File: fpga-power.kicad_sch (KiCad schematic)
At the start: 118 parts, among them U3002 XC7K160T-FFG676

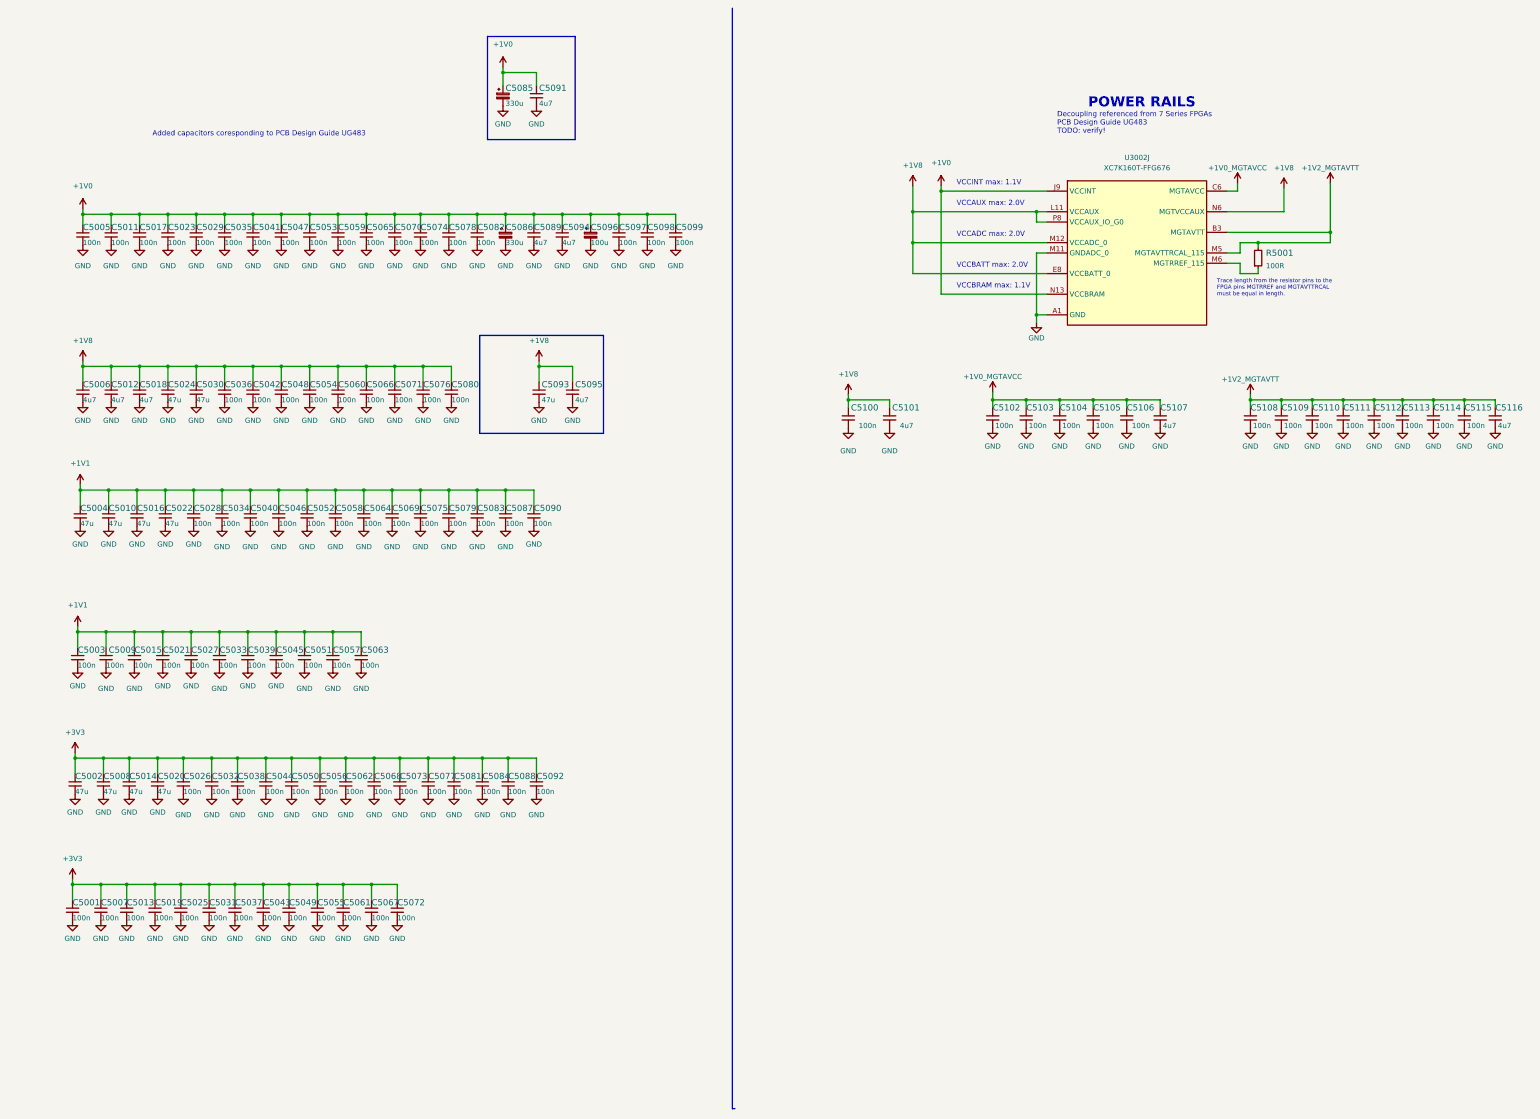
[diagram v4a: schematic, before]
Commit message: Create FPGA decoupling, start creating power planes
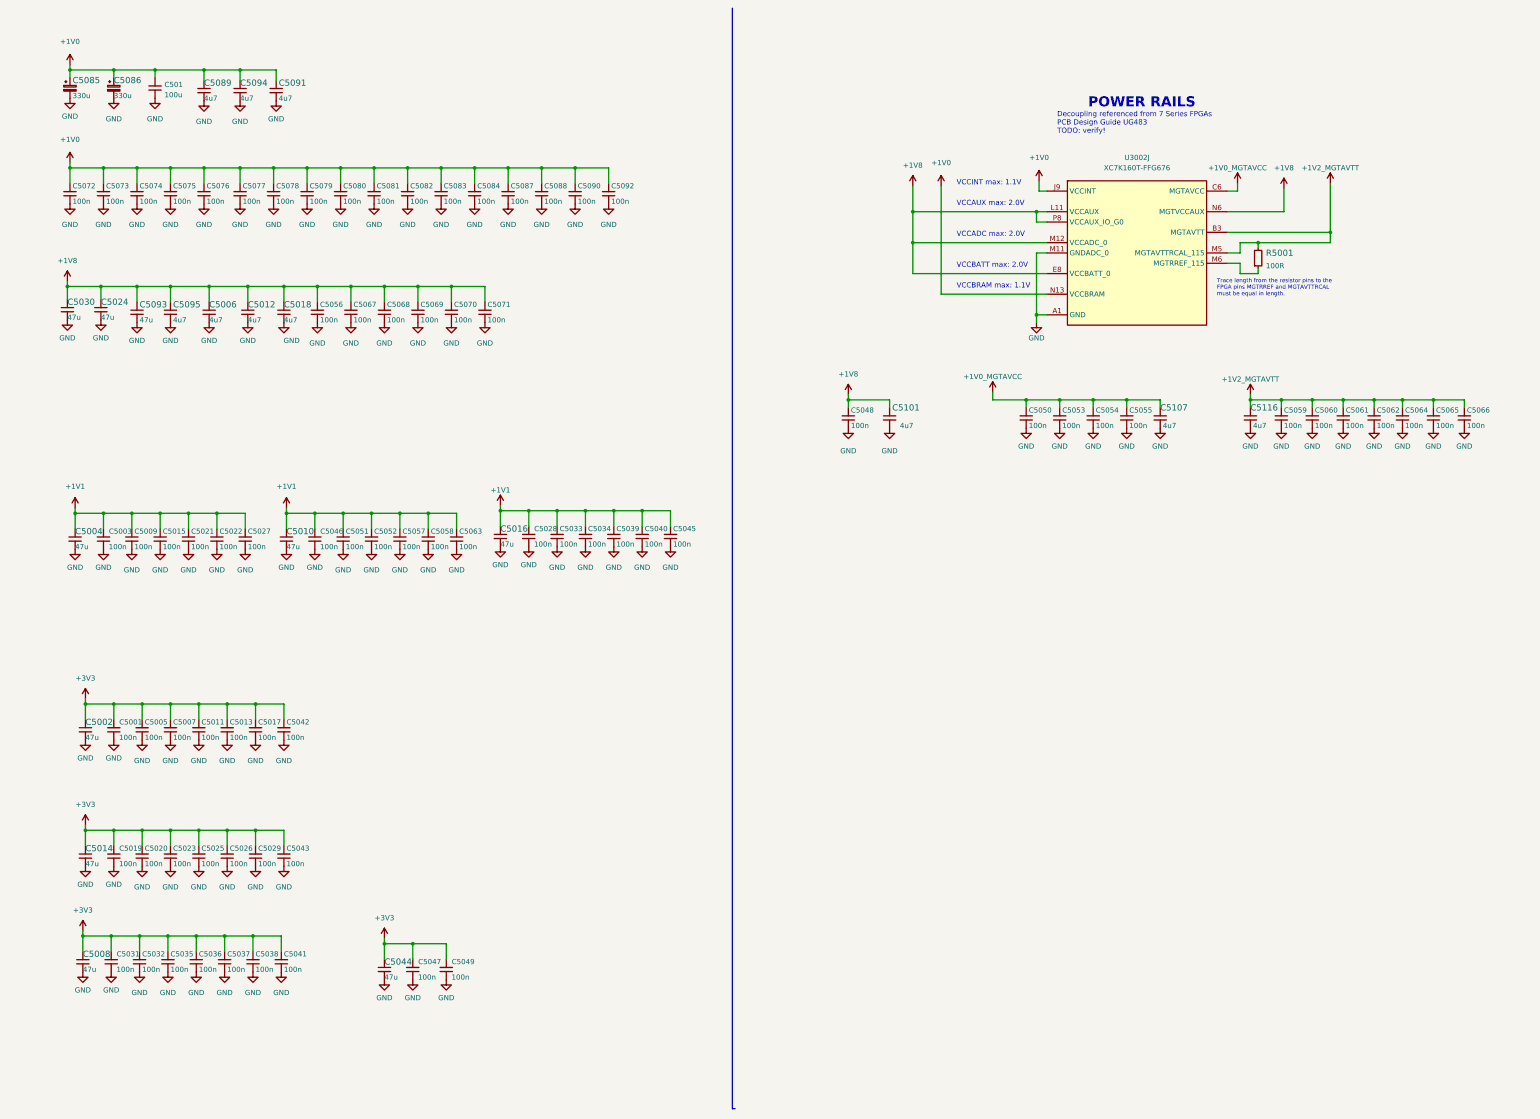
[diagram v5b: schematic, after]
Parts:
- removed C5001, C5003, C5005, C5007, C5009, C5011, C5013, C5015, C5017, C5019, C5021, C5023, C5025, C5026, C5027, C5028, C5029, C5031, C5032, C5033, C5034, C5035, C5036, C5037, C5038, C5039, C5040, C5041, C5042, C5043, C5044, C5045, C5046, C5047, C5048, C5049, C5050, C5051, C5052, C5053, C5054, C5055, C5056, C5057, C5058, C5059, C5060, C5061, C5062, C5063, C5064, C5065, C5066, C5067, C5068, C5069, C5070, C5071, C5072, C5073, C5074, C5075, C5076, C5077, C5078, C5079, C5080, C5081, C5082, C5083, C5084, C5087, C5088, C5092, C5097, C5098, C5099, C5100, C5102, C5103, C5104, C5105, C5106, C5109, C5110, C5111, C5112, C5113, C5114, C5115: C_100n_0201, data-center-rdimm-ddr4-tester-footprints:C_0201, symbol data-center-rdimm-ddr4-tester:C_100n_0201
- removed C5020, C5022: C_47u_0603, data-center-rdimm-ddr4-tester-footprints:C_0603_1608Metric, symbol data-center-rdimm-ddr4-tester:C_47u_0603
- removed C5090, C5108: C_100n_0402, data-center-rdimm-ddr4-tester-footprints:C_0402_1005Metric, symbol data-center-rdimm-ddr4-tester:C_100n_0402
- removed C5096: C_100u_KEMET_A, data-center-rdimm-ddr4-tester-footprints:KEMET_A, symbol data-center-rdimm-ddr4-tester:C_100u_KEMET_A
- added C5001, C5003, C5005, C5007, C5009, C5011, C5013, C5015, C5017, C5019, C5020, C5021, C5022, C5023, C5025, C5026, C5027, C5028, C5029, C5031, C5032, C5033, C5034, C5035, C5036, C5037, C5038, C5039, C5040, C5041, C5042, C5043, C5045, C5046, C5047, C5048, C5049, C5050, C5051, C5052, C5053, C5054, C5055, C5056, C5057, C5058, C5059, C5060, C5061, C5062, C5063, C5064, C5065, C5066, C5067, C5068, C5069, C5070, C5071, C5072, C5073, C5074, C5075, C5076, C5077, C5078, C5079, C5080, C5081, C5082, C5083, C5084, C5087, C5088, C5090, C5092: C_100n_0402, antmicro-footprints:C_0402_1005Metric_EIA, symbol antmicroCapacitors0402:C_100n_0402
- added C501: C_100u_0805, antmicro-footprints:C_0805_2012Metric, symbol antmicroCapacitorsmisc:C_100u_0805
- added C5044: C_47u_0603, data-center-rdimm-ddr4-tester-footprints:C_0603_1608Metric, symbol data-center-rdimm-ddr4-tester:C_47u_0603
- C5006, C5012, C5018, C5089, C5091, C5094, C5095, C5101, C5107, C5116: footprint data-center-rdimm-ddr4-tester-footprints:C_0402_1005Metric -> antmicro-footprints:C_0402_1005Metric_EIA
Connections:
- net +1V0: now also C501.2, C5072.2, C5073.2, C5074.2, C5075.2, C5076.2, C5077.2, C5078.2, C5079.2, C5080.2, C5081.2, C5082.2, C5083.2, C5084.2, C5087.2, C5088.2, C5090.2, C5092.2
- net +1V0_MGTAVCC: now also C5050.2, C5053.2, C5054.2, C5055.2
- net +1V1: now also C5003.2, C5009.2, C5015.2, C5021.2, C5022.2, C5027.2, C5028.2, C5033.2, C5034.2, C5039.2, C5040.2, C5045.2, C5046.2, C5051.2, C5052.2, C5057.2, C5058.2, C5063.2
- net +1V2_MGTAVTT: now also C5059.2, C5060.2, C5061.2, C5062.2, C5064.2, C5065.2, C5066.2
- net +1V8: now also C5048.2, C5056.2, C5067.2, C5068.2, C5069.2, C5070.2, C5071.2
- net +3V3: now also C5001.2, C5005.2, C5007.2, C5011.2, C5013.2, C5017.2, C5019.2, C5020.2, C5023.2, C5025.2, C5026.2, C5029.2, C5031.2, C5032.2, C5035.2, C5036.2, C5037.2, C5038.2, C5041.2, C5042.2, C5043.2, C5044.1, C5047.2, C5049.2
- net GND: now also C5001.1, C5003.1, C5005.1, C5007.1, C5009.1, C501.1, C5011.1, C5013.1, C5015.1, C5017.1, C5019.1, C5020.1, C5021.1, C5022.1, C5023.1, C5025.1, C5026.1, C5027.1, C5028.1, C5029.1, C5031.1, C5032.1, C5033.1, C5034.1, C5035.1, C5036.1, C5037.1, C5038.1, C5039.1, C5040.1, C5041.1, C5042.1, C5043.1, C5044.2, C5045.1, C5046.1, C5047.1, C5048.1, C5049.1, C5050.1, C5051.1, C5052.1, C5053.1, C5054.1, C5055.1, C5056.1, C5057.1, C5058.1, C5059.1, C5060.1, C5061.1, C5062.1, C5063.1, C5064.1, C5065.1, C5066.1, C5067.1, C5068.1, C5069.1, C5070.1, C5071.1, C5072.1, C5073.1, C5074.1, C5075.1, C5076.1, C5077.1, C5078.1, C5079.1, C5080.1, C5081.1, C5082.1, C5083.1, C5084.1, C5087.1, C5088.1, C5090.1, C5092.1
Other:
- note removed: "Added capacitors coresponding to PCB Design Guide UG483"
- moved on the sheet: C5002, C5004, C5006, C5008, C5010, C5012, C5014, C5016, C5018, C5024, C5030, C5085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

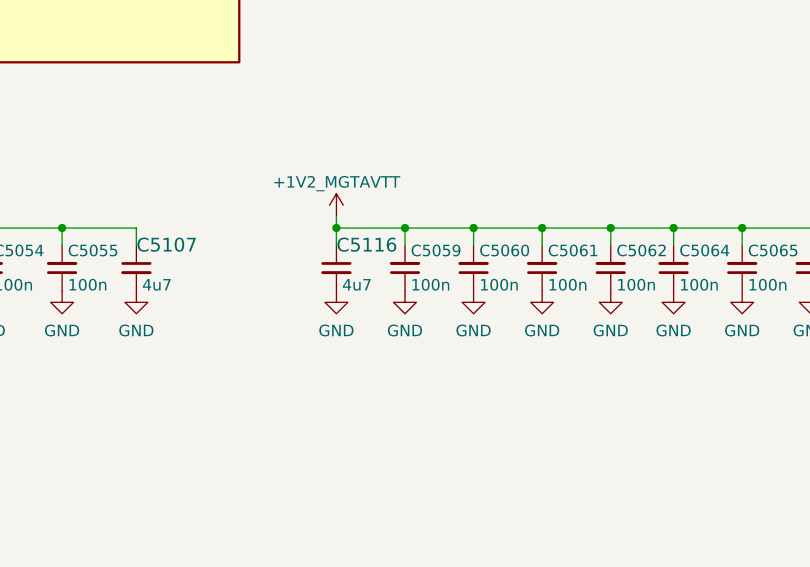
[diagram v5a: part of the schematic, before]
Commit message: Improve DDR assigment, connect ECC to remaining pins, cleanup not used components, continue placement of misc. components
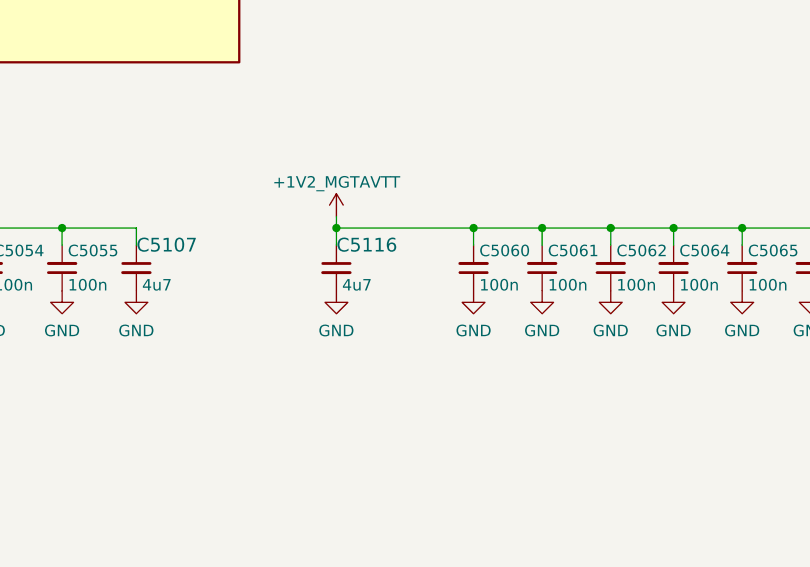
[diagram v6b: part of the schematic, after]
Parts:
- removed C5059: C_100n_0402, antmicro-footprints:C_0402_1005Metric_EIA, symbol antmicroCapacitors0402:C_100n_0402
- R5001: footprint data-center-rdimm-ddr4-tester-footprints:R_0402_1005Metric -> antmicro-footprints:R_0402_1005Metric_EIA
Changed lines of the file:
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@@
   (junction (at 52.705 184.15) (diameter 0) (color 0 0 0 0)
   )
-  (junction (at 326.39 109.22) (diameter 0) (color 0 0 0 0)
-  )
   (junction (at 44.45 81.28) (diameter 0) (color 0 0 0 0)
   )
@@
     (stroke (width 0) (type default) (color 0 0 0 0))
   )
-  (wire (pts (xy 326.39 109.22) (xy 334.01 109.22))
-    (stroke (width 0) (type default) (color 0 0 0 0))
-  )
   (wire (pts (xy 140.97 136.525) (xy 133.985 136.525))
     (stroke (width 0) (type default) (color 0 0 0 0))
@@
     (stroke (width 0) (type default) (color 0 0 0 0))
   )
-  (wire (pts (xy 318.77 109.22) (xy 326.39 109.22))
+  (wire (pts (xy 318.77 109.22) (xy 334.01 109.22))
     (stroke (width 0) (type default) (color 0 0 0 0))
   )
@@
     (stroke (width 0) (type default) (color 0 0 0 0))
   )
-  (wire (pts (xy 326.39 109.22) (xy 326.39 111.125))
-    (stroke (width 0) (type default) (color 0 0 0 0))
-  )
   (wire (pts (xy 356.235 109.22) (xy 363.855 109.22))
     (stroke (width 0) (type default) (color 0 0 0 0))
@@
     (pin "1")
   )
-  (symbol (lib_id "antmicroCapacitors0402:C_100n_0402") (at 326.39 116.205 90) (unit 1)
-    (in_bom yes) (on_board yes)
-    (property "Reference" "C5059" (id 0) (at 327.025 111.76 90)
-      (effects (font (size 1.27 1.27) (thickness 0.15)) (justify right))
-    )
-    (property "Value" "C_100n_0402" (id 1) (at 336.55 95.885 0)
-      (effects (font (size 1.27 1.27) (thickness 0.15)) (justify left bottom) hide)
-    )
-    (property "Footprint" "antmicro-footprints:C_0402_1005Metric_EIA" (id 2) (at 339.09 95.885 0)
-      (effects (font (size 1.27 1.27) (thickness 0.15)) (justify left bottom) hide)
-    )
-    (property "Datasheet" "https://www.murata.com/products/productdetail?partno=GRM155R61H104KE14%23" (id 3) (at 341.63 95.885 0)
-      (effects (font (size 1.27 1.27) (thickness 0.15)) (justify left bottom) hide)
-    )
-    (property "MPN" "GRM155R61H104KE14D" (id 4) (at 344.17 95.885 0)
-      (effects (font (size 1.27 1.27) (thickness 0.15)) (justify left bottom) hide)
-    )
-    (property "Manufacturer" "Murata" (id 5) (at 346.71 95.885 0)
-      (effects (font (size 1.27 1.27) (thickness 0.15)) (justify left bottom) hide)
-    )
-    (property "License" "Apache-2.0" (id 6) (at 349.25 95.885 0)
-      (effects (font (size 1.27 1.27) (thickness 0.15)) (justify left bottom) hide)
-    )
-    (property "Author" "Antmicro" (id 7) (at 351.79 95.885 0)
-      (effects (font (size 1.27 1.27) (thickness 0.15)) (justify left bottom) hide)
-    )
-    (property "Val" "100n" (id 8) (at 327.025 115.57 90)
-      (effects (font (size 1.27 1.27) (thickness 0.15)) (justify right))
-    )
-    (property "Voltage" "50V" (id 9) (at 354.33 95.885 0)
-      (effects (font (size 1.27 1.27)) (justify left bottom) hide)
-    )
-    (property "Dielectric" "X5R" (id 10) (at 356.87 95.885 0)
-      (effects (font (size 1.27 1.27)) (justify left bottom) hide)
-    )
-    (pin "1")
-    (pin "2")
-  )
   (symbol (lib_id "data-center-rdimm-ddr4-tester:GND") (at 52.705 60.96 0) (unit 1)
     (in_bom yes) (on_board yes) (fields_autoplaced)
@@
       (effects (font (size 1.27 1.27) (thickness 0.15)) (justify left bottom) hide)
     )
-    (property "Footprint" "data-center-rdimm-ddr4-tester-footprints:R_0402_1005Metric" (id 2) (at 335.915 56.515 0)
+    (property "Footprint" "antmicro-footprints:R_0402_1005Metric_EIA" (id 2) (at 335.915 56.515 0)
       (effects (font (size 1.27 1.27) (thickness 0.15)) (justify left bottom) hide)
     )
@@
     (pin "2")
   )
-  (symbol (lib_id "data-center-rdimm-ddr4-tester:GND") (at 326.39 116.205 0) (unit 1)
-    (in_bom yes) (on_board yes) (fields_autoplaced)
-    (property "Reference" "#PWR05110" (id 0) (at 326.39 122.555 0)
-      (effects (font (size 1.27 1.27)) hide)
-    )
-    (property "Value" "GND" (id 1) (at 326.39 120.65 0))
-    (property "Footprint" "" (id 2) (at 326.39 116.205 0)
-      (effects (font (size 1.27 1.27)) hide)
-    )
-    (property "Datasheet" "" (id 3) (at 326.39 116.205 0)
-      (effects (font (size 1.27 1.27)) hide)
-    )
-    (property "Author" "Antmicro" (id 4) (at 335.28 123.825 0)
-      (effects (font (size 1.27 1.27) (thickness 0.15)) (justify left bottom) hide)
-    )
-    (property "License" "Apache-2.0" (id 5) (at 335.28 126.365 0)
-      (effects (font (size 1.27 1.27) (thickness 0.15)) (justify left bottom) hide)
-    )
-    (pin "1")
-  )
   (symbol (lib_id "data-center-rdimm-ddr4-tester:GND") (at 52.07 250.19 0) (unit 1)

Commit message: Add loclib
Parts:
- C5001, C5003, C5005, C5007, C5009, C5011, C5013, C5015, C5017, C5019, C5020, C5021, C5022, C5023, C5025, C5026, C5027, C5028, C5029, C5031, C5032, C5033, C5034, C5035, C5036, C5037, C5038, C5039, C5040, C5041, C5042, C5043, C5045, C5046, C5047, C5048, C5049, C5050, C5051, C5052, C5053, C5054, C5055, C5056, C5057, C5058, C5060, C5061, C5062, C5063, C5064, C5065, C5066, C5067, C5068, C5069, C5070, C5071, C5072, C5073, C5074, C5075, C5076, C5077, C5078, C5079, C5080, C5081, C5082, C5083, C5084, C5087, C5088, C5090, C5092: footprint antmicro-footprints:C_0402_1005Metric_EIA -> sodimm-ddr5-tester-footprints:C_0402_1005Metric_EIA; symbol antmicroCapacitors0402:C_100n_0402 -> sodimm-ddr5-tester:C_100n_0402
- C5002, C5004, C5008, C5010, C5014, C5016, C5024, C5030, C5044, C5093: footprint data-center-rdimm-ddr4-tester-footprints:C_0603_1608Metric -> sodimm-ddr5-tester-footprints:C_0603_1608Metric; symbol data-center-rdimm-ddr4-tester:C_47u_0603 -> sodimm-ddr5-tester:C_47u_0603
- C5006, C5012, C5018, C5089, C5091, C5094, C5095, C5101, C5107, C5116: footprint antmicro-footprints:C_0402_1005Metric_EIA -> sodimm-ddr5-tester-footprints:C_0402_1005Metric_EIA; symbol data-center-rdimm-ddr4-tester:C_4u7_0402 -> sodimm-ddr5-tester:C_4u7_0402
- C501: footprint antmicro-footprints:C_0805_2012Metric -> sodimm-ddr5-tester-footprints:C_0805_2012Metric; symbol antmicroCapacitorsmisc:C_100u_0805 -> sodimm-ddr5-tester:C_100u_0805
- C5085, C5086: footprint data-center-rdimm-ddr4-tester-footprints:KEMET_D -> sodimm-ddr5-tester-footprints:KEMET_D; symbol data-center-rdimm-ddr4-tester:C_330u_KEMET_D -> sodimm-ddr5-tester:C_330u_KEMET_D
- R5001: footprint antmicro-footprints:R_0402_1005Metric_EIA -> sodimm-ddr5-tester-footprints:R_0402_1005Metric_EIA; symbol data-center-rdimm-ddr4-tester:R_100R_0402 -> sodimm-ddr5-tester:R_100R_0402
- U3002: footprint data-center-rdimm-ddr4-tester-footprints:BGA-676_27x27mm_Layout26x26_P1X1mm -> sodimm-ddr5-tester-footprints:BGA-676_27x27mm_Layout26x26_P1X1mm; symbol data-center-rdimm-ddr4-tester:XC7K160T-FFG676 -> sodimm-ddr5-tester:XC7K160T-FFG676
